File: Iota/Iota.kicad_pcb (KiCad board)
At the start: 2 copper layers, 19 parts, among them J1 USB_B_Mini, J2 Conn_01x12_Male, J3 Conn_01x12_Male, J4 Conn_01x05_Male, SW1 SW_DIP_x01, U1 ATmega32U4-AU, Y1 16MHz

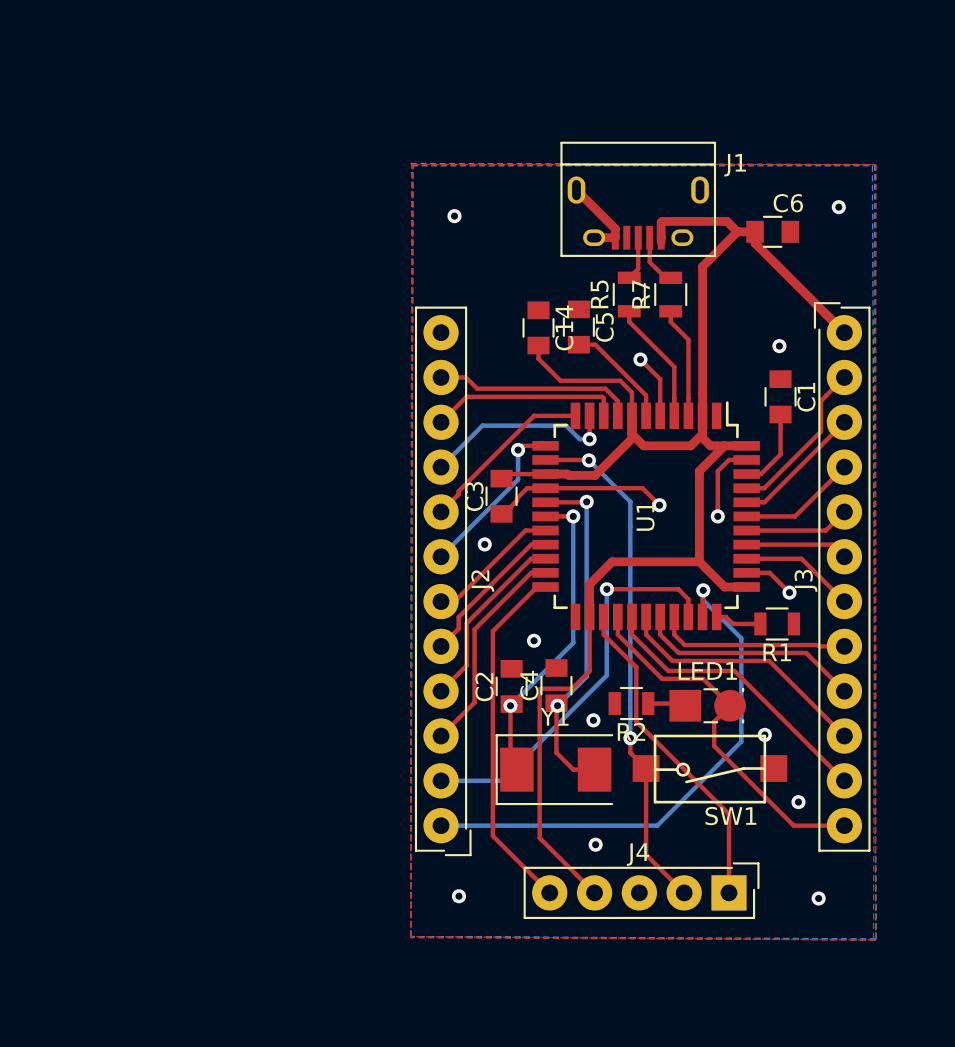
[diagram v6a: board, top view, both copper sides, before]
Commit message: Checking traces, footprint sizing
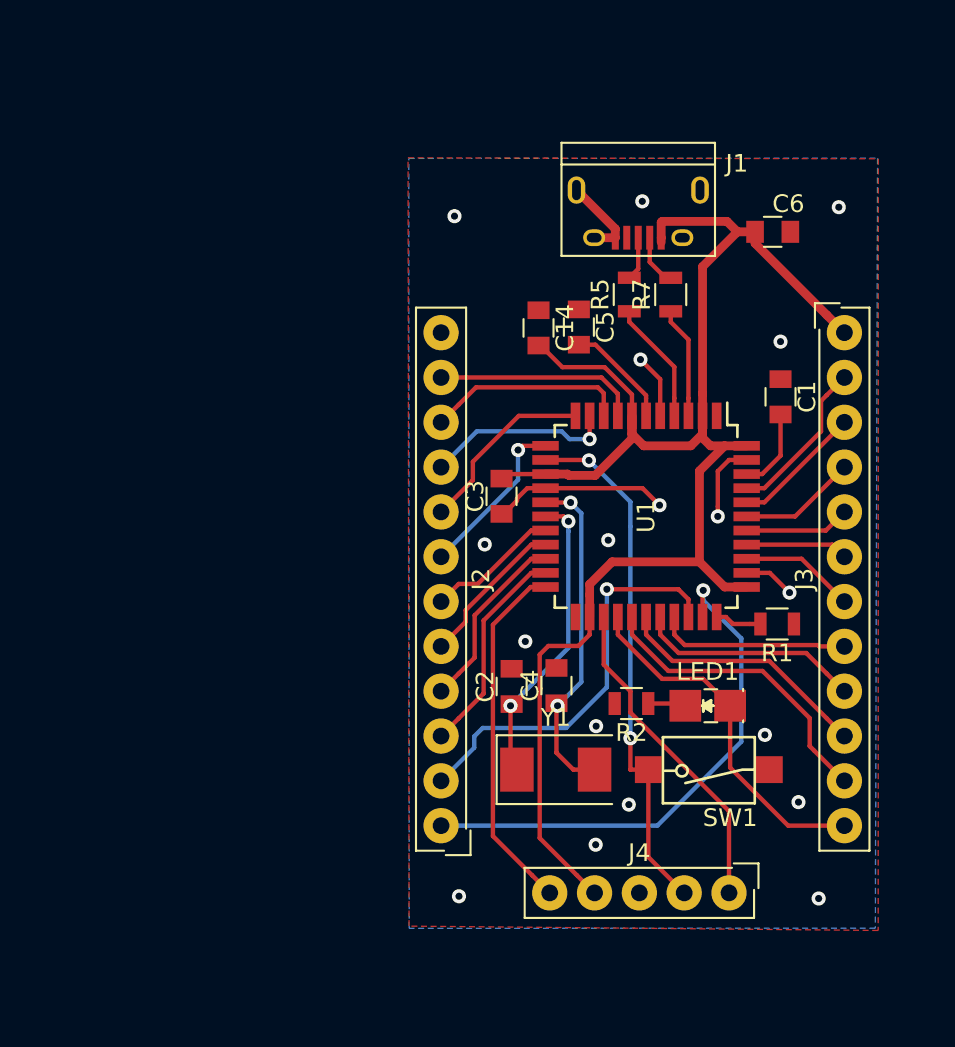
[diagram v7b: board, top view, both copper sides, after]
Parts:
- moved SW1 0.09 mm to (137.4, 96.2)
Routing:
- net D7: track 16.5 -> 17.4 mm
- net Net-(C4-Pad1): track 19.9 -> 19.1 mm
- net C6: track 22.6 -> 23.4 mm
- net B1: track 10.8 -> 11.5 mm
- net D6: track 20.9 -> 20.4 mm
- net Net-(C2-Pad1): track 17.5 -> 17.0 mm
- net B3: track 9.98 -> 10.5 mm
- net GND: vias 15 -> 18

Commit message: Adding in F+B silkscreen markings
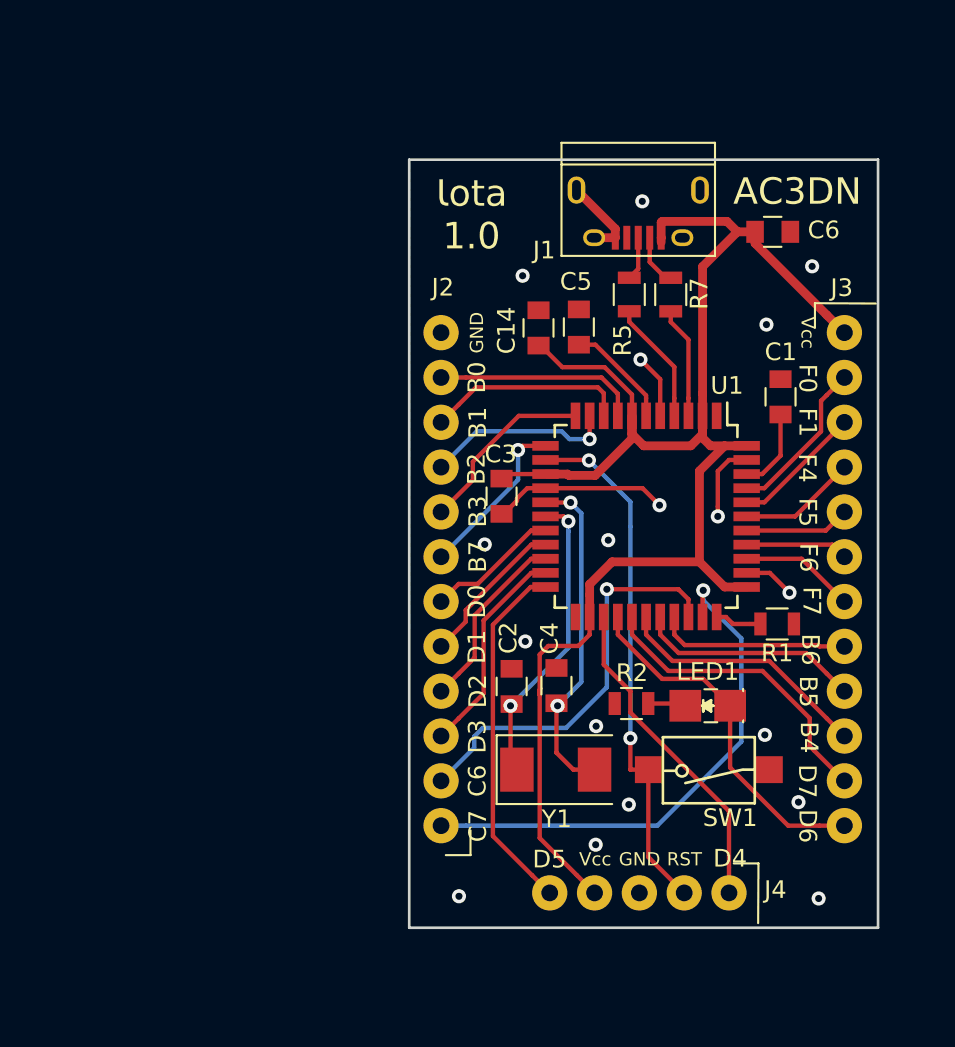
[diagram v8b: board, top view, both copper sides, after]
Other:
- board outline added: 26.6 x 43.5 mm
- board text added: "AC3DN"
- board text added: "B0"
- board text added: "B1"
- board text added: "B2"
- board text added: "B3"
- board text added: "B4"
- board text added: "B5"
- board text added: "B6"
- board text added: "B7"
- board text added: "C6"
- board text added: "C7"
- board text added: "D0"
- board text added: "D1"
- board text added: "D2"
- board text added: "D3"
- board text added: "D4"
- board text added: "D5"
- board text added: "D6"
- board text added: "D7"
- board text added: "F0"
- board text added: "F1"
- board text added: "F4"
- board text added: "F5"
- board text added: "F6"
- board text added: "F7"
- board text added: "GND"
- board text added: "RST"
- board text added: "Vcc"
- board text added: "Ɩota 1.0"
